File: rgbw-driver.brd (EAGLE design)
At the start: 66 x 19.4 mm, 16 parts, among them J1 M20, J2 M20, Q1 IRLL014, Q2 IRLL014, Q3 IRLL014, Q4 IRLL014, X1 2PIN

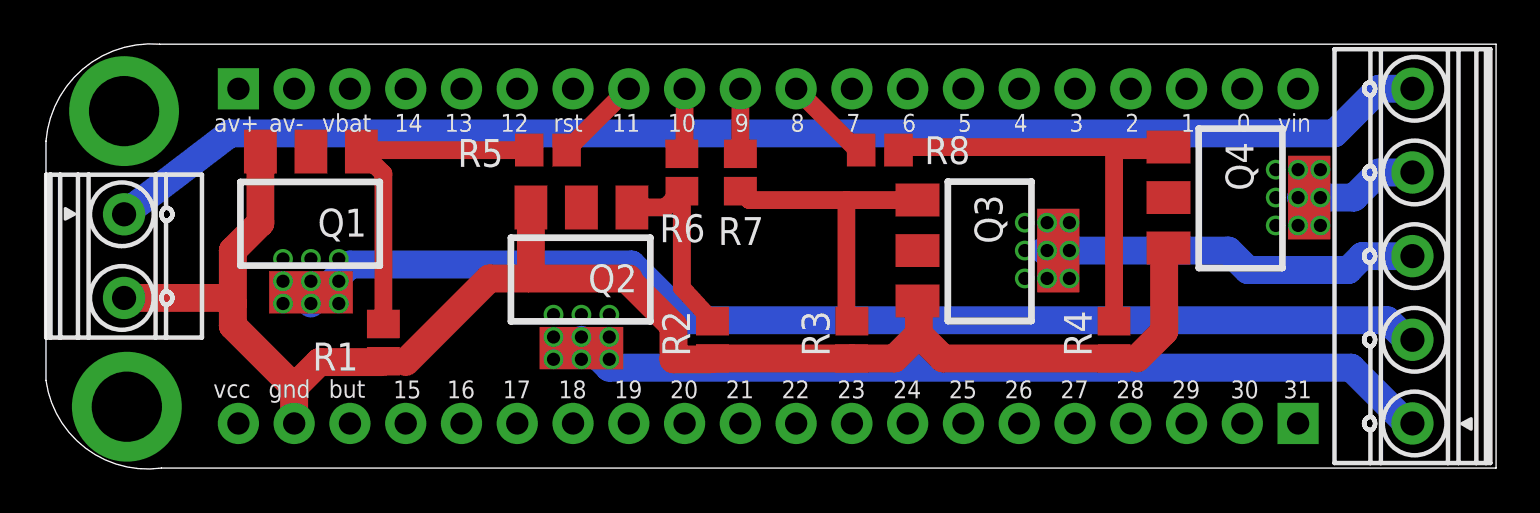
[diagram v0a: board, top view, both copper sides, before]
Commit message: RGBW traces now are polygonal pours for heat dissipation
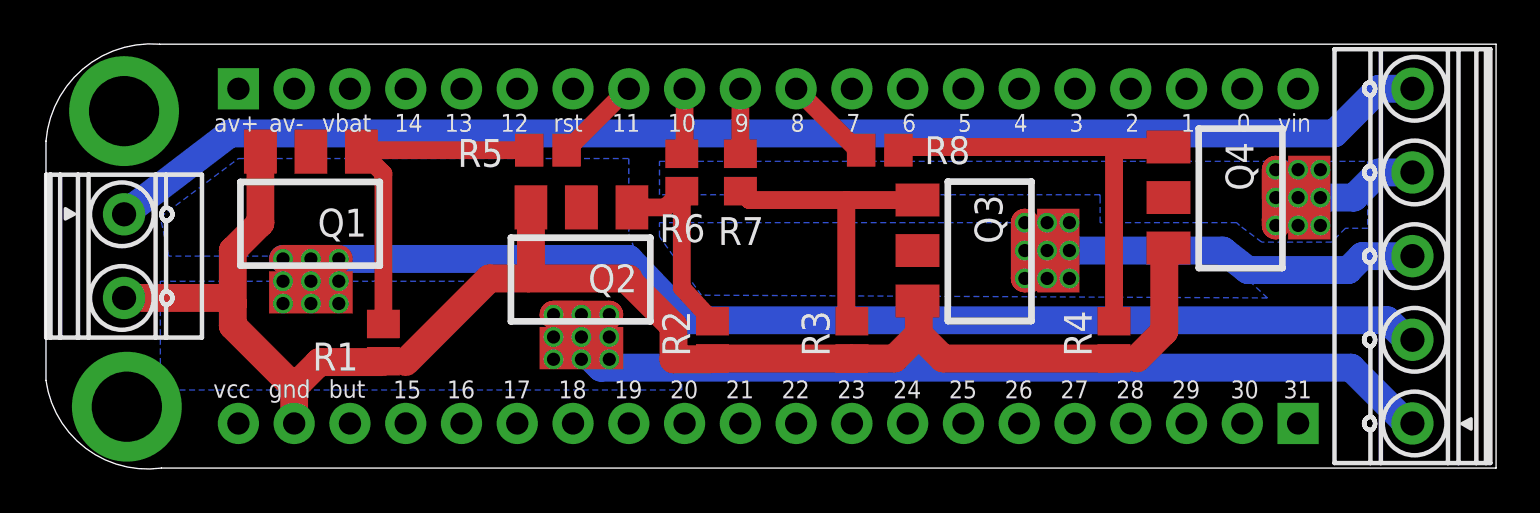
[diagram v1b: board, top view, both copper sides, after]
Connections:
- net N$31 renamed V+
- removed net N$50: Q1.2, U$1.2
- removed net N$51: Q2.2, U$1.1
- removed net N$52: Q3.2, U$1.3
- removed net N$53: Q4.2, U$1.4
- new net B: Q1.4, U$1.2
- new net G: U$1.4
- new net R: Q3.4, U$1.3
- new net W: Q2.4, U$1.1
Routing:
- net B: track 0.00 -> 57.1 mm, vias 0 -> 9
- net N$50: track 52.3 -> 0.00 mm
- net W: track 0.00 -> 46.6 mm, vias 0 -> 9
- net N$51: track 39.4 -> 0.00 mm
- net R: track 0.00 -> 23.5 mm, vias 0 -> 9
- net N$52: track 17.4 -> 0.00 mm
- net G: track 0.00 -> 11.2 mm, vias 0 -> 9
- net N$53: track 5.55 -> 0.00 mm
- added copper zone on layer 16, net B
- added copper zone on layer 16, net G
- added copper zone on layer 16, net R
- added copper zone on layer 16, net W

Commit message: Minor schematic and silkscreen improvements
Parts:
- Q1, Q2, Q3, Q4: value IRLL014 -> STN4NF03L
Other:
- board text added: "B"
- board text added: "G"
- board text added: "GND"
- board text added: "R"
- board text added: "V+"
- board text added: "W"
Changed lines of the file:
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@@
 <text x="57.5056" y="3.302" size="0.8128" layer="121" font="vector" ratio="16">31</text>
 <text x="24.257" y="15.4432" size="0.8128" layer="121" font="vector" ratio="16">rst</text>
+<text x="66.802" y="16.9672" size="1.016" layer="122" font="vector" ratio="16" rot="MR0">V+</text>
+<text x="66.294" y="13.0302" size="1.016" layer="122" font="vector" ratio="16" rot="MR0">G</text>
+<text x="66.294" y="9.2202" size="1.016" layer="122" font="vector" ratio="16" rot="MR0">R</text>
+<text x="66.294" y="5.4102" size="1.016" layer="122" font="vector" ratio="16" rot="MR0">B</text>
+<text x="66.294" y="1.6002" size="1.016" layer="122" font="vector" ratio="16" rot="MR0">W</text>
+<text x="8.5598" y="12.827" size="1.016" layer="121" font="vector" ratio="16" rot="R270">V+</text>
+<text x="8.5598" y="9.398" size="1.016" layer="121" font="vector" ratio="16" rot="R270">GND</text>
 </plain>
 <attributes>
@@
 <attribute name="VALUE" x="21.717" y="13.716" size="1.27" layer="27" rot="R180"/>
 </element>
-<element name="Q1" library="transistors" package="SOT-223" value="IRLL014" x="13.208" y="11.303" smashed="yes" rot="R180">
+<element name="Q1" library="transistors" package="SOT-223" value="STN4NF03L" x="13.208" y="11.303" smashed="yes" rot="R180">
 <attribute name="NAME" x="15.748" y="11.938" size="1.27" layer="21" ratio="10" rot="R180"/>
 </element>
@@
 <attribute name="VALUE" x="19.939" y="5.842" size="1.27" layer="27" rot="R180"/>
 </element>
-<element name="Q2" library="transistors" package="SOT-223" value="IRLL014" x="25.527" y="8.763" smashed="yes" rot="R180">
+<element name="Q2" library="transistors" package="SOT-223" value="STN4NF03L" x="25.527" y="8.763" smashed="yes" rot="R180">
 <attribute name="NAME" x="28.067" y="9.398" size="1.27" layer="21" ratio="10" rot="R180"/>
 </element>
-<element name="Q3" library="transistors" package="SOT-223" value="IRLL014" x="44.069" y="10.033" smashed="yes" rot="R270">
+<element name="Q3" library="transistors" package="SOT-223" value="STN4NF03L" x="44.069" y="10.033" smashed="yes" rot="R270">
 <attribute name="NAME" x="43.434" y="12.573" size="1.27" layer="21" ratio="10" rot="R270"/>
 </element>
-<element name="Q4" library="transistors" package="SOT-223" value="IRLL014" x="55.499" y="12.446" smashed="yes" rot="R270">
+<element name="Q4" library="transistors" package="SOT-223" value="STN4NF03L" x="55.499" y="12.446" smashed="yes" rot="R270">
 <attribute name="NAME" x="54.864" y="14.986" size="1.27" layer="21" ratio="10" rot="R270"/>
 </element>

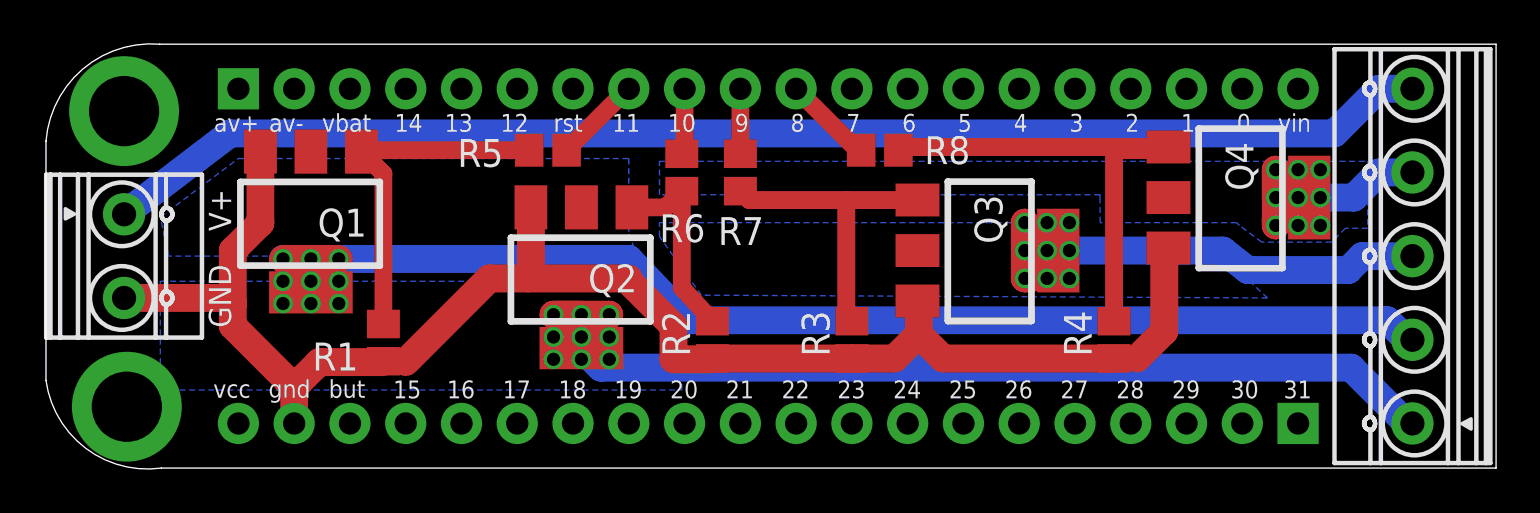
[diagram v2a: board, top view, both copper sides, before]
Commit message: Added power indicator LED
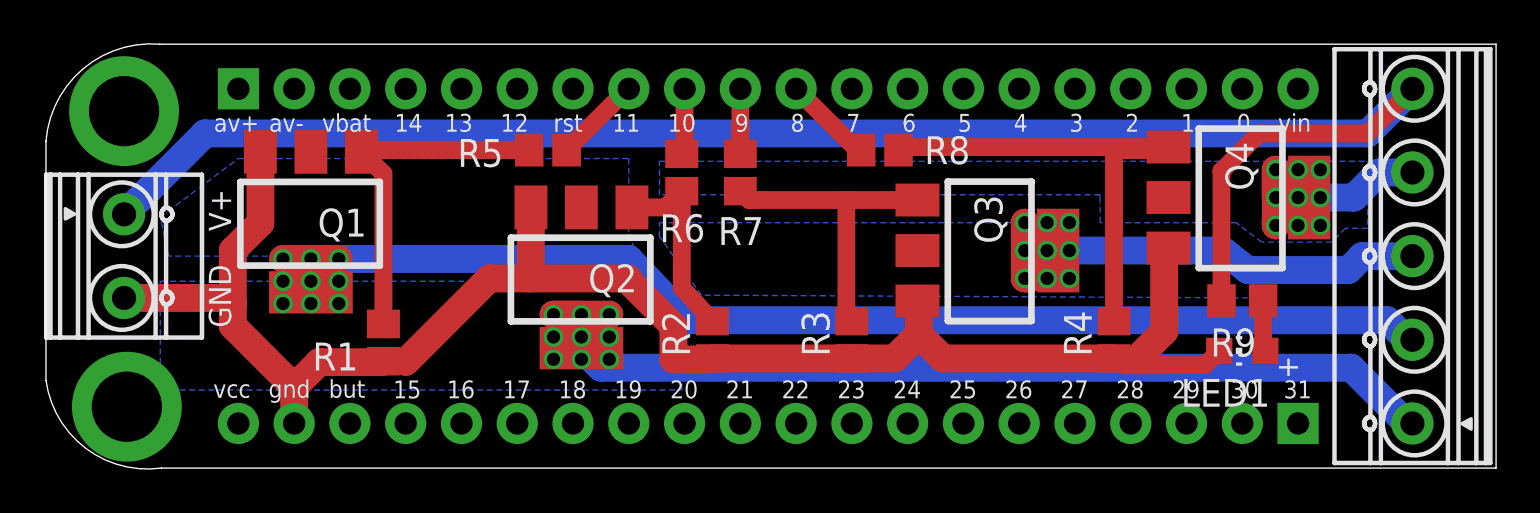
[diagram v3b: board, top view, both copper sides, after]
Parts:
- added LED1: (no value), adafruit:CHIP-LED0805
- added R9: 1K, rcl:R0805
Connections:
- removed net V+: U$1.5, X1.1
- new net N$3: LED1.A, R9.1
- new net N$6: R9.2, U$1.5, X1.1
- net N$4: now also LED1.C
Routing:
- net N$6: track 0.00 -> 77.2 mm
- net V+: track 60.8 -> 0.00 mm
- net N$4: track 73.6 -> 77.8 mm
- net N$3: track 0.00 -> 2.36 mm
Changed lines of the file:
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@@
 <layer number="54" name="bGND_GNDA" color="1" fill="9" visible="no" active="no"/>
 <layer number="56" name="wert" color="7" fill="1" visible="yes" active="yes"/>
+<layer number="57" name="tCAD" color="7" fill="1" visible="no" active="no"/>
 <layer number="91" name="Nets" color="2" fill="1" visible="no" active="no"/>
 <layer number="92" name="Busses" color="1" fill="1" visible="no" active="no"/>
@@
 <layer number="97" name="Info" color="7" fill="1" visible="no" active="no"/>
 <layer number="98" name="Guide" color="6" fill="1" visible="no" active="no"/>
+<layer number="99" name="SpiceOrder" color="7" fill="1" visible="no" active="no"/>
 <layer number="100" name="Muster" color="7" fill="1" visible="no" active="no"/>
 <layer number="101" name="Patch_Top" color="12" fill="4" visible="yes" active="yes"/>
@@
 <layer number="106" name="bPlate" color="7" fill="1" visible="yes" active="yes"/>
 <layer number="107" name="Crop" color="7" fill="1" visible="yes" active="yes"/>
+<layer number="108" name="fp8" color="7" fill="1" visible="no" active="yes"/>
+<layer number="109" name="fp9" color="7" fill="1" visible="no" active="yes"/>
+<layer number="110" name="fp0" color="7" fill="1" visible="no" active="yes"/>
+<layer number="111" name="LPC17xx" color="7" fill="1" visible="no" active="yes"/>
+<layer number="112" name="tSilk" color="7" fill="1" visible="no" active="yes"/>
+<layer number="113" name="ReferenceLS" color="7" fill="1" visible="no" active="no"/>
 <layer number="116" name="Patch_BOT" color="9" fill="4" visible="yes" active="yes"/>
+<layer number="118" name="Rect_Pads" color="7" fill="1" visible="no" active="no"/>
 <layer number="121" name="_tsilk" color="14" fill="1" visible="yes" active="yes"/>
 <layer number="122" name="_bsilk" color="14" fill="1" visible="yes" active="yes"/>
+<layer number="123" name="tTestmark" color="7" fill="1" visible="no" active="yes"/>
+<layer number="124" name="bTestmark" color="7" fill="1" visible="no" active="yes"/>
+<layer number="125" name="_tNames" color="7" fill="1" visible="no" active="yes"/>
+<layer number="126" name="_bNames" color="7" fill="1" visible="no" active="yes"/>
+<layer number="127" name="_tValues" color="7" fill="1" visible="no" active="yes"/>
+<layer number="128" name="_bValues" color="7" fill="1" visible="no" active="yes"/>
+<layer number="131" name="tAdjust" color="7" fill="1" visible="no" active="yes"/>
+<layer number="132" name="bAdjust" color="7" fill="1" visible="no" active="yes"/>
+<layer number="144" name="Drill_legend" color="7" fill="1" visible="no" active="yes"/>
+<layer number="150" name="Notes" color="7" fill="1" visible="no" active="yes"/>
 <layer number="151" name="HeatSink" color="7" fill="1" visible="yes" active="yes"/>
+<layer number="152" name="_bDocu" color="7" fill="1" visible="no" active="yes"/>
+<layer number="153" name="FabDoc1" color="6" fill="1" visible="no" active="no"/>
+<layer number="154" name="FabDoc2" color="2" fill="1" visible="no" active="no"/>
+<layer number="155" name="FabDoc3" color="7" fill="15" visible="no" active="no"/>
 <layer number="199" name="Contour" color="7" fill="1" visible="yes" active="yes"/>
 <layer number="200" name="200bmp" color="1" fill="10" visible="yes" active="yes"/>
@@
 <layer number="207" name="207bmp" color="8" fill="10" visible="yes" active="yes"/>
 <layer number="208" name="208bmp" color="9" fill="10" visible="yes" active="yes"/>
+<layer number="209" name="209bmp" color="7" fill="1" visible="no" active="yes"/>
+<layer number="210" name="210bmp" color="7" fill="1" visible="no" active="yes"/>
+<layer number="211" name="211bmp" color="7" fill="1" visible="no" active="yes"/>
+<layer number="212" name="212bmp" color="7" fill="1" visible="no" active="yes"/>
+<layer number="213" name="213bmp" color="7" fill="1" visible="no" active="yes"/>
+<layer number="214" name="214bmp" color="7" fill="1" visible="no" active="yes"/>
+<layer number="215" name="215bmp" color="7" fill="1" visible="no" active="yes"/>
+<layer number="216" name="216bmp" color="7" fill="1" visible="no" active="yes"/>
+<layer number="217" name="217bmp" color="18" fill="1" visible="no" active="no"/>
+<layer number="218" name="218bmp" color="19" fill="1" visible="no" active="no"/>
+<layer number="219" name="219bmp" color="20" fill="1" visible="no" active="no"/>
+<layer number="220" name="220bmp" color="21" fill="1" visible="no" active="no"/>
+<layer number="221" name="221bmp" color="22" fill="1" visible="no" active="no"/>
+<layer number="222" name="222bmp" color="23" fill="1" visible="no" active="no"/>
+<layer number="223" name="223bmp" color="24" fill="1" visible="no" active="no"/>
+<layer number="224" name="224bmp" color="25" fill="1" visible="no" active="no"/>
+<layer number="231" name="Eagle3D_PG1" color="7" fill="1" visible="no" active="no"/>
+<layer number="232" name="Eagle3D_PG2" color="7" fill="1" visible="no" active="no"/>
+<layer number="233" name="Eagle3D_PG3" color="7" fill="1" visible="no" active="no"/>
+<layer number="248" name="Housing" color="7" fill="1" visible="no" active="yes"/>
+<layer number="249" name="Edge" color="7" fill="1" visible="no" active="yes"/>
 <layer number="250" name="Descript" color="3" fill="1" visible="no" active="no"/>
 <layer number="251" name="SMDround" color="12" fill="11" visible="no" active="no"/>
@@
 <attribute name="OC_FARNELL" value="3704592" x="4.699" y="5.969" size="1.778" layer="27" rot="R270" display="off"/>
 </element>
+<element name="R9" library="rcl" package="R0805" value="1K" x="55.626" y="7.747" rot="R180"/>
+<element name="LED1" library="adafruit" package="CHIP-LED0805" value="" x="55.626" y="5.461" rot="R90"/>
 </elements>
 <signals>
@@
 <wire x1="49.784" y1="5.119" x2="41.998" y2="5.119" width="1.27" layer="1"/>
 <wire x1="41.998" y1="5.119" x2="40.894" y2="6.223" width="1.27" layer="1"/>
-<wire x1="49.784" y1="5.119" x2="50.839" y2="5.119" width="0.8128" layer="1"/>
-<wire x1="50.839" y1="5.119" x2="52.07" y2="6.35" width="1.27" layer="1"/>
 <wire x1="52.07" y1="6.35" x2="52.07" y2="9.952" width="1.27" layer="1"/>
 <wire x1="52.07" y1="9.952" x2="52.264" y2="10.146" width="0.8128" layer="1"/>
@@
 <wire x1="4.699" y1="7.874" x2="9.398" y2="7.874" width="1.27" layer="1"/>
 <wire x1="9.398" y1="7.874" x2="9.652" y2="7.62" width="1.27" layer="1"/>
+<contactref element="LED1" pad="C"/>
+<wire x1="49.872" y1="5.207" x2="50.253" y2="4.826" width="0.8128" layer="1"/>
+<wire x1="50.253" y1="4.826" x2="51.054" y2="4.826" width="0.8128" layer="1"/>
+<wire x1="51.054" y1="4.826" x2="53.941" y2="4.826" width="0.8128" layer="1"/>
+<wire x1="53.941" y1="4.826" x2="54.576" y2="5.461" width="0.8128" layer="1"/>
+<wire x1="52.07" y1="6.35" x2="51.054" y2="5.334" width="1.27" layer="1"/>
+<wire x1="51.054" y1="5.334" x2="51.054" y2="4.826" width="0.8128" layer="1"/>
 </signal>
 <signal name="N$8">
@@
 </polygon>
 </signal>
-<signal name="V+" airwireshidden="yes">
+<signal name="N$35">
+<via x="4.699" y="16.383" extent="1-16" drill="3.2004" diameter="5.0038"/>
+</signal>
+<signal name="N$39">
+<via x="4.826" y="2.921" extent="1-16" drill="3.2004" diameter="5.0038"/>
+</signal>
+<signal name="N$3">
+<contactref element="R9" pad="1"/>
+<contactref element="LED1" pad="A"/>
+<wire x1="56.576" y1="7.747" x2="56.576" y2="5.488" width="0.8128" layer="1"/>
+<wire x1="56.576" y1="5.488" x2="56.676" y2="5.461" width="0.8128" layer="1"/>
+</signal>
+<signal name="N$6">
 <contactref element="U$1" pad="5"/>
 <contactref element="X1" pad="1"/>
-<wire x1="63.373" y1="17.399" x2="61.849" y2="17.399" width="1.27" layer="16"/>
-<wire x1="61.849" y1="17.399" x2="59.817" y2="15.367" width="1.27" layer="16"/>
-<wire x1="59.817" y1="15.367" x2="9.525" y2="15.367" width="1.27" layer="16"/>
-<wire x1="9.525" y1="15.367" x2="4.699" y2="11.684" width="1.27" layer="16"/>
-</signal>
-<signal name="N$35">
-<via x="4.699" y="16.383" extent="1-16" drill="3.2004" diameter="5.0038"/>
-</signal>
-<signal name="N$39">
-<via x="4.826" y="2.921" extent="1-16" drill="3.2004" diameter="5.0038"/>
+<contactref element="R9" pad="2"/>
+<wire x1="4.699" y1="11.684" x2="8.382" y2="15.367" width="1.27" layer="16"/>
+<wire x1="8.382" y1="15.367" x2="61.341" y2="15.367" width="1.27" layer="16"/>
+<wire x1="61.341" y1="15.367" x2="63.373" y2="17.399" width="1.27" layer="16"/>
+<wire x1="54.676" y1="7.747" x2="54.676" y2="13.655" width="0.8128" layer="1"/>
+<wire x1="54.676" y1="13.655" x2="56.388" y2="15.367" width="0.8128" layer="1"/>
+<wire x1="56.388" y1="15.367" x2="61.341" y2="15.367" width="0.8128" layer="1"/>
+<wire x1="61.341" y1="15.367" x2="63.373" y2="17.399" width="0.8128" layer="1"/>
 </signal>
 </signals>
